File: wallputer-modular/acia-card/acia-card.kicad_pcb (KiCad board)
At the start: 2 copper layers, 99.7 x 99.7 mm, 1 part

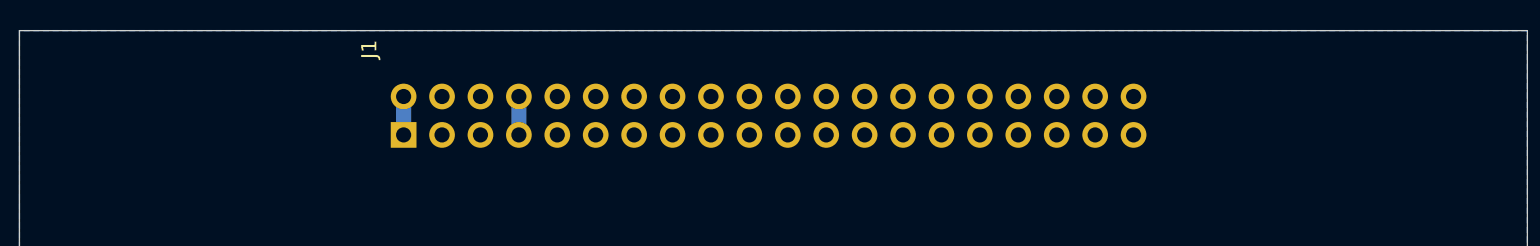
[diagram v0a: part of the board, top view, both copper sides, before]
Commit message: add card name
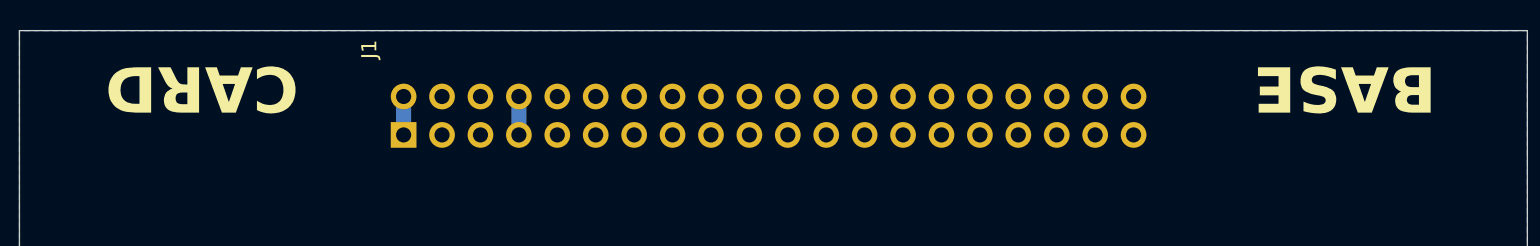
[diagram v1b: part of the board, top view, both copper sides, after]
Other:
- board text added: "BASE"
- board text added: "CARD"
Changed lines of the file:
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@@
 		(layer "Edge.Cuts")
+	)
+	(gr_text "BASE"
+		(at 151.13 67.31 180)
+		(layer "F.SilkS")
+		(effects
+			(font
+				(size 3 3)
+				(thickness 0.5)
+				(bold yes)
+			)
+		)
+	)
+	(gr_text "CARD\n"
+		(at 75.565 67.31 180)
+		(layer "F.SilkS")
+		(effects
+			(font
+				(size 3 3)
+				(thickness 0.5)
+				(bold yes)
+			)
+		)
 	)
 	(segment

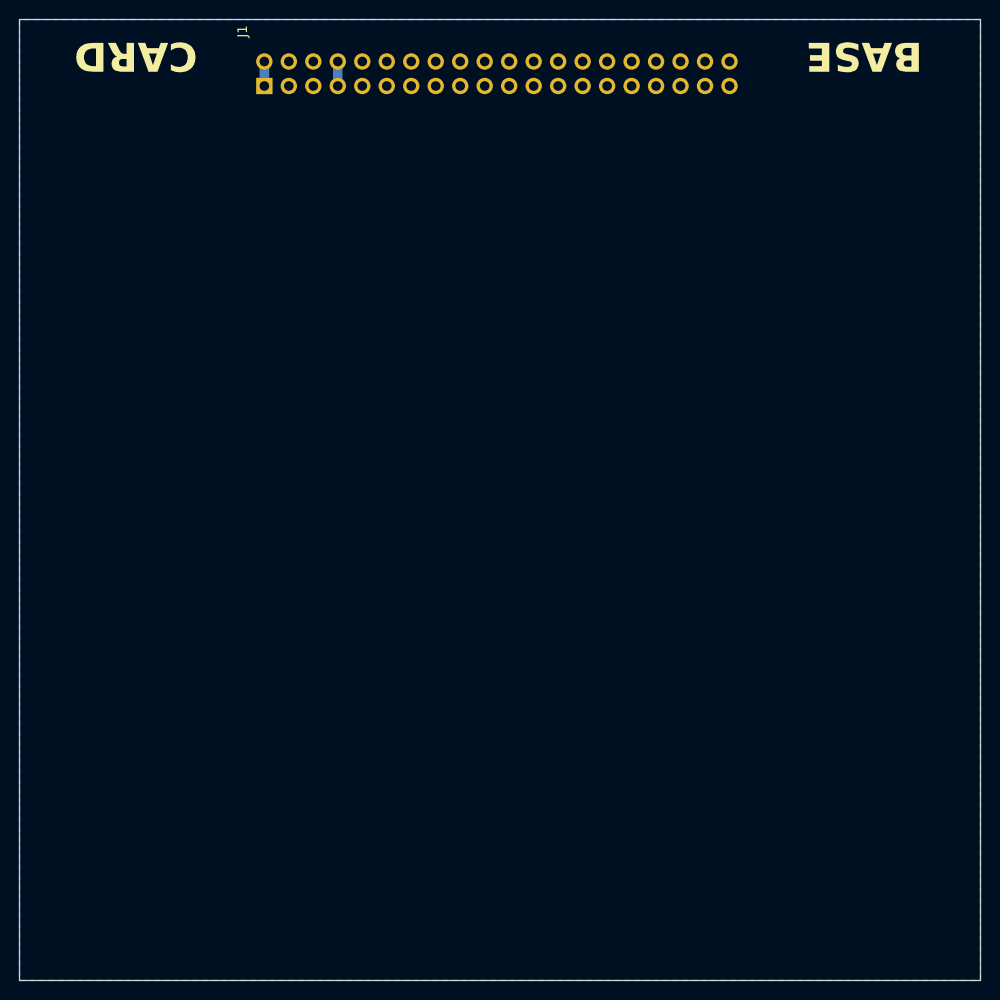
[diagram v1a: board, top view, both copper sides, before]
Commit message: implement acia card
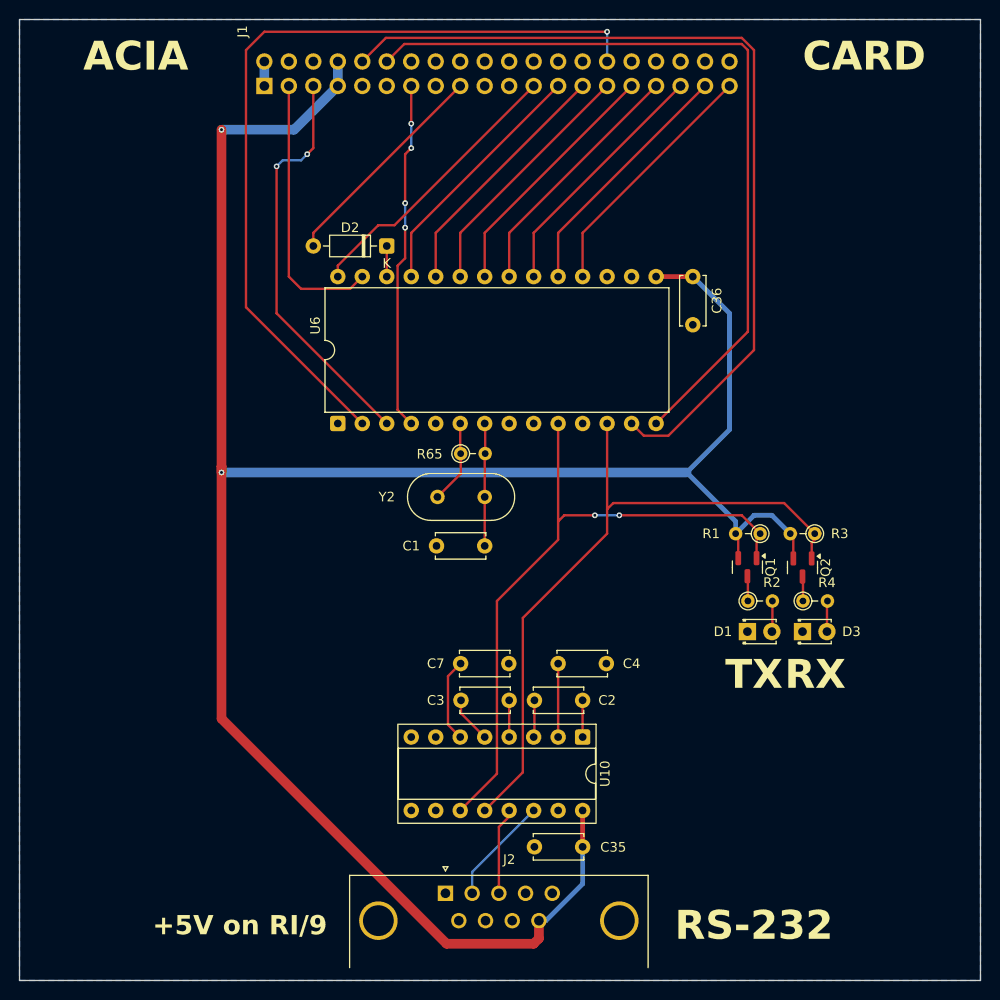
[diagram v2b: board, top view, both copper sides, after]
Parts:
- added C1: 20pf, Capacitor_THT:C_Disc_D5.0mm_W2.5mm_P5.00mm, F.Cu at (111.8, 118.1)
- added C2: 1uF, Capacitor_THT:C_Disc_D5.0mm_W2.5mm_P5.00mm, F.Cu at (121.9, 134.1)
- added C3: 1uF, Capacitor_THT:C_Disc_D5.0mm_W2.5mm_P5.00mm, F.Cu at (114.3, 134.1)
- added C35: 100nF, Capacitor_THT:C_Disc_D5.0mm_W2.5mm_P5.00mm, F.Cu at (121.9, 149.3)
- added C36: 100nF, Capacitor_THT:C_Disc_D5.0mm_W2.5mm_P5.00mm, F.Cu at (133.3, 90.2)
- added C4: 1uF, Capacitor_THT:C_Disc_D5.0mm_W2.5mm_P5.00mm, F.Cu at (119.4, 130.3)
- added C7: 1uF, Capacitor_THT:C_Disc_D5.0mm_W2.5mm_P5.00mm, F.Cu at (109.3, 130.3)
- added D1: Red, LED_THT:LED_D1.8mm_W3.3mm_H2.4mm, F.Cu at (139.0, 127.0)
- added D2: 1N4148, Diode_THT:D_DO-35_SOD27_P7.62mm_Horizontal, F.Cu at (101.6, 87.0)
- added D3: Green, LED_THT:LED_D1.8mm_W3.3mm_H2.4mm, F.Cu at (144.7, 127.0)
- added J2: DE9_Socket, Connector_Dsub:DSUB-9_Pins_Horizontal_P2.77x2.84mm_EdgePinOffset4.94mm_Housed_MountingHolesOffset4.94mm, F.Cu at (107.7, 154.1)
- added Q1: BSS84, Package_TO_SOT_SMD:SOT-23, F.Cu at (139.0, 120.3)
- added Q2: BSS84, Package_TO_SOT_SMD:SOT-23, F.Cu at (144.7, 120.3)
- added R1: 100k, Resistor_THT:R_Axial_DIN0204_L3.6mm_D1.6mm_P2.54mm_Vertical, F.Cu at (140.3, 116.8)
- added R2: 220, Resistor_THT:R_Axial_DIN0204_L3.6mm_D1.6mm_P2.54mm_Vertical, F.Cu at (139.1, 123.8)
- added R3: 100k, Resistor_THT:R_Axial_DIN0204_L3.6mm_D1.6mm_P2.54mm_Vertical, F.Cu at (146.0, 116.8)
- added R4: 220, Resistor_THT:R_Axial_DIN0204_L3.6mm_D1.6mm_P2.54mm_Vertical, F.Cu at (144.8, 123.8)
- added R65: 1M, Resistor_THT:R_Axial_DIN0204_L3.6mm_D1.6mm_P2.54mm_Vertical, F.Cu at (109.3, 108.5)
- added U10: MAX232, Package_DIP:DIP-16_W7.62mm_Socket, F.Cu at (121.9, 137.9)
- added U6: W65C51NxP, Package_DIP:DIP-28_W15.24mm, F.Cu at (96.5, 105.4)
- added Y2: 1.8432Mhz, Crystal:Crystal_HC18-U_Vertical, F.Cu at (111.8, 113.0)
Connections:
- J1 pad 10: unconnected-(J1-A5-Pad10) -> /A5
- J1 pad 11: unconnected-(J1-A6-Pad11) -> /A6
- J1 pad 12: unconnected-(J1-A7-Pad12) -> /A7
- J1 pad 13: unconnected-(J1-A8-Pad13) -> /A8
- J1 pad 14: unconnected-(J1-A9-Pad14) -> /A9
- J1 pad 15: unconnected-(J1-A10-Pad15) -> /A10
- J1 pad 16: unconnected-(J1-A11-Pad16) -> /A11
- J1 pad 17: unconnected-(J1-A12-Pad17) -> /A12
- J1 pad 18: unconnected-(J1-A13-Pad18) -> /A13
- J1 pad 19: unconnected-(J1-A14-Pad19) -> /A14
- J1 pad 20: unconnected-(J1-A15-Pad20) -> /A15
- J1 pad 21: unconnected-(J1-D0-Pad21) -> /D0
- J1 pad 22: unconnected-(J1-D1-Pad22) -> /D1
- J1 pad 23: unconnected-(J1-D2-Pad23) -> /D2
- J1 pad 24: unconnected-(J1-D3-Pad24) -> /D3
- J1 pad 25: unconnected-(J1-D4-Pad25) -> /D4
- J1 pad 26: unconnected-(J1-D5-Pad26) -> /D5
- J1 pad 27: unconnected-(J1-D6-Pad27) -> /D6
- J1 pad 28: unconnected-(J1-D7-Pad28) -> /D7
- J1 pad 29: unconnected-(J1-RW/-Pad29) -> RW/
- J1 pad 32: unconnected-(J1-IRQ/-Pad32) -> IRQ/
- J1 pad 34: unconnected-(J1-RES/-Pad34) -> RES/
- J1 pad 38: unconnected-(J1-ACC/-Pad38) -> ACC/
- J1 pad 39: unconnected-(J1-CLK-Pad39) -> CLK
- J1 pad 5: unconnected-(J1-A0-Pad5) -> /A0
- J1 pad 6: unconnected-(J1-A1-Pad6) -> /A1
- J1 pad 7: unconnected-(J1-A2-Pad7) -> /A2
- J1 pad 8: unconnected-(J1-A3-Pad8) -> /A3
- J1 pad 9: unconnected-(J1-A4-Pad9) -> /A4
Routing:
- net +5V: track 2.54 -> 233.5 mm, vias 0 -> 2
- net /A0: track 0.00 -> 90.2 mm
- net /A10: track 0.00 -> 85.1 mm, vias 0 -> 1
- net /A1: track 0.00 -> 81.2 mm
- net Net-(Q2-G): track 0.00 -> 71.5 mm
- net Net-(Q1-G): track 0.00 -> 69.0 mm, vias 0 -> 2
- net ACC/: track 0.00 -> 42.4 mm, vias 0 -> 2
- net RES/: track 0.00 -> 36.2 mm, vias 0 -> 4
- net RW/: track 0.00 -> 29.2 mm
- net CLK: track 0.00 -> 28.4 mm
- net /D2: track 0.00 -> 26.1 mm
- net /D1: track 0.00 -> 26.1 mm
- net /D7: track 0.00 -> 26.1 mm
- net /D6: track 0.00 -> 26.1 mm
- net /D5: track 0.00 -> 26.1 mm
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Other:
- board text added: "+5V on RI/9"
- board text added: "ACIA"
- board text added: "RS-232"
- board text added: "RX"
- board text added: "TX"
- board text removed: "BASE"

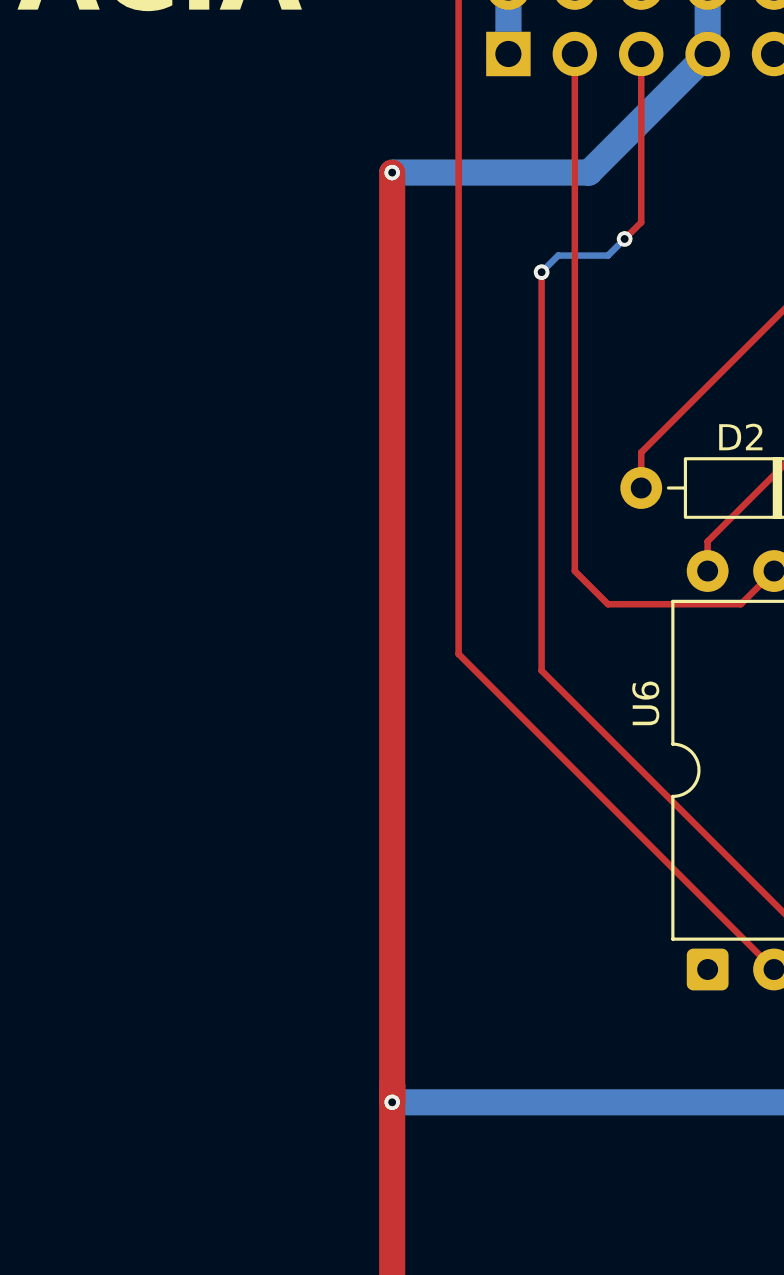
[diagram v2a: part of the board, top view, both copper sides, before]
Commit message: implement via board
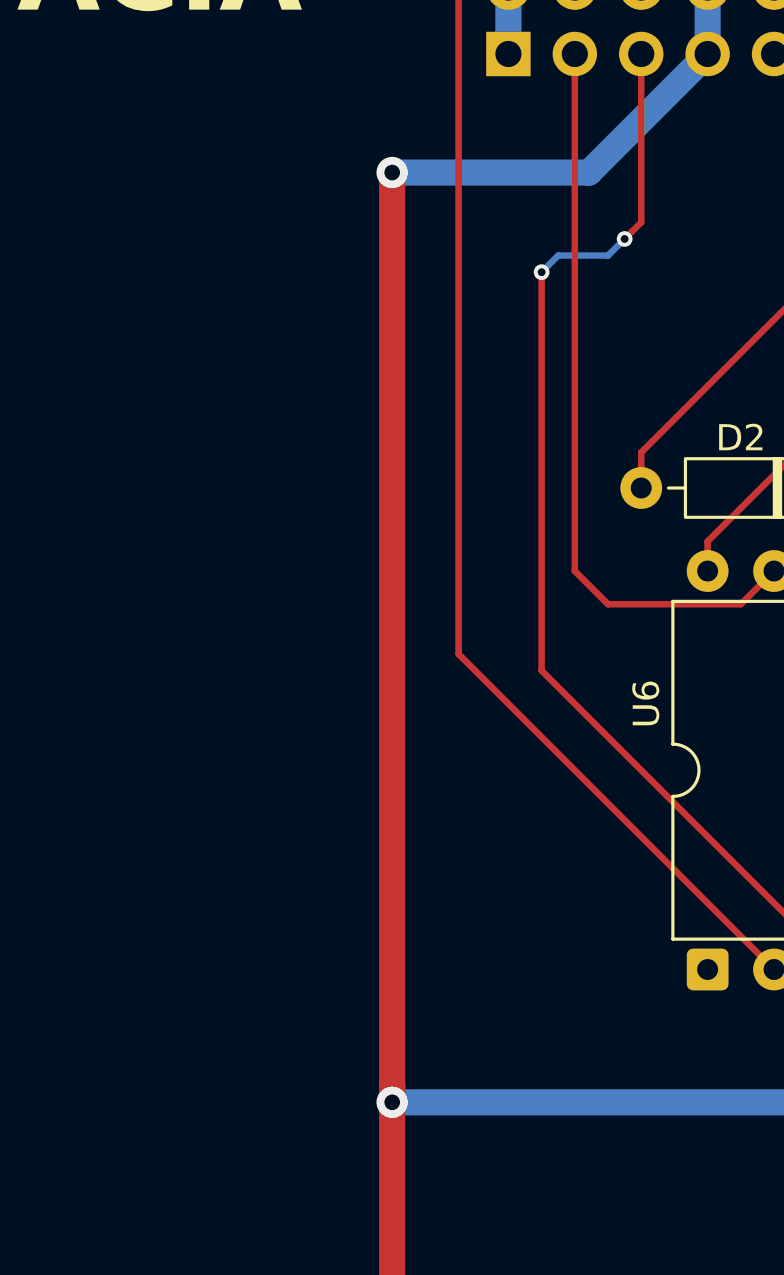
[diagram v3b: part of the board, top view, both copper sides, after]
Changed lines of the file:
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@@
 	(via
 		(at 84.455 110.49)
-		(size 0.6)
-		(drill 0.3)
+		(size 1.2)
+		(drill 0.6)
 		(layers "F.Cu" "B.Cu")
 		(net 38)
@@
 	(via
 		(at 84.455 74.93)
-		(size 0.6)
-		(drill 0.3)
+		(size 1.2)
+		(drill 0.6)
 		(layers "F.Cu" "B.Cu")
 		(net 38)
